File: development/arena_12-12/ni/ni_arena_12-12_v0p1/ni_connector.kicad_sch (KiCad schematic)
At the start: 1 part, among them J2 NI_TE_68pos

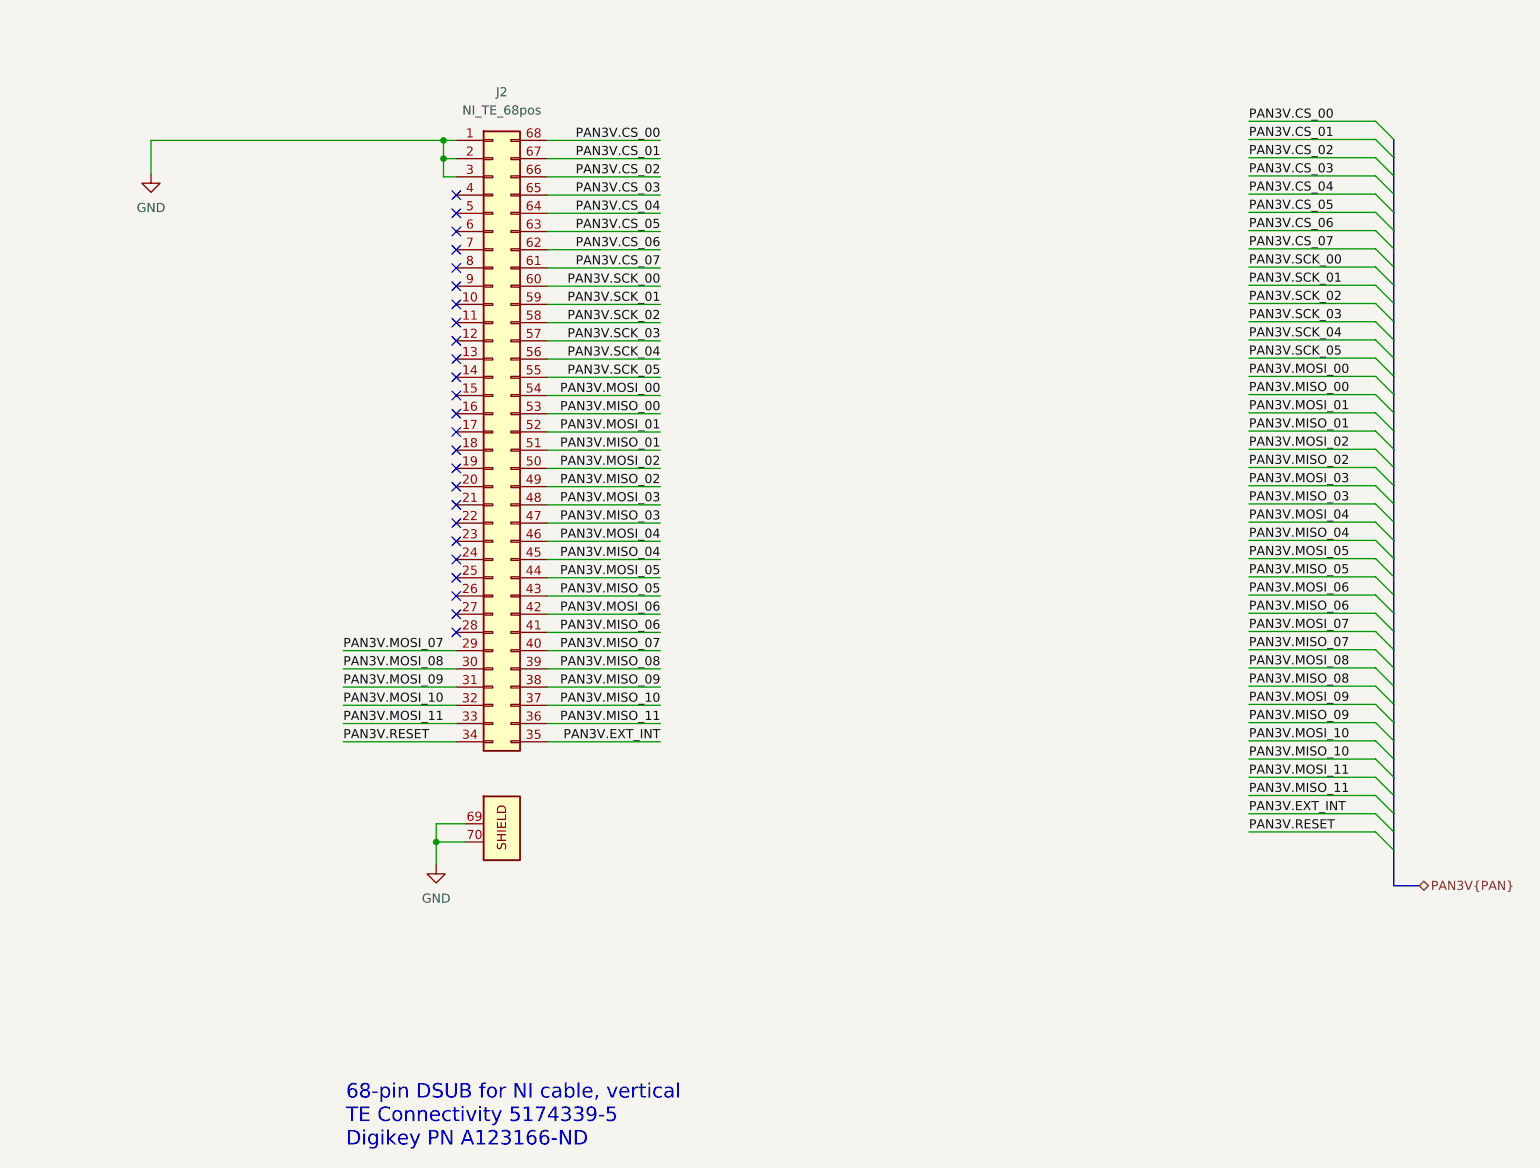
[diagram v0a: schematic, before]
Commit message: Worked on schematic adding series termination resistors and buffers.
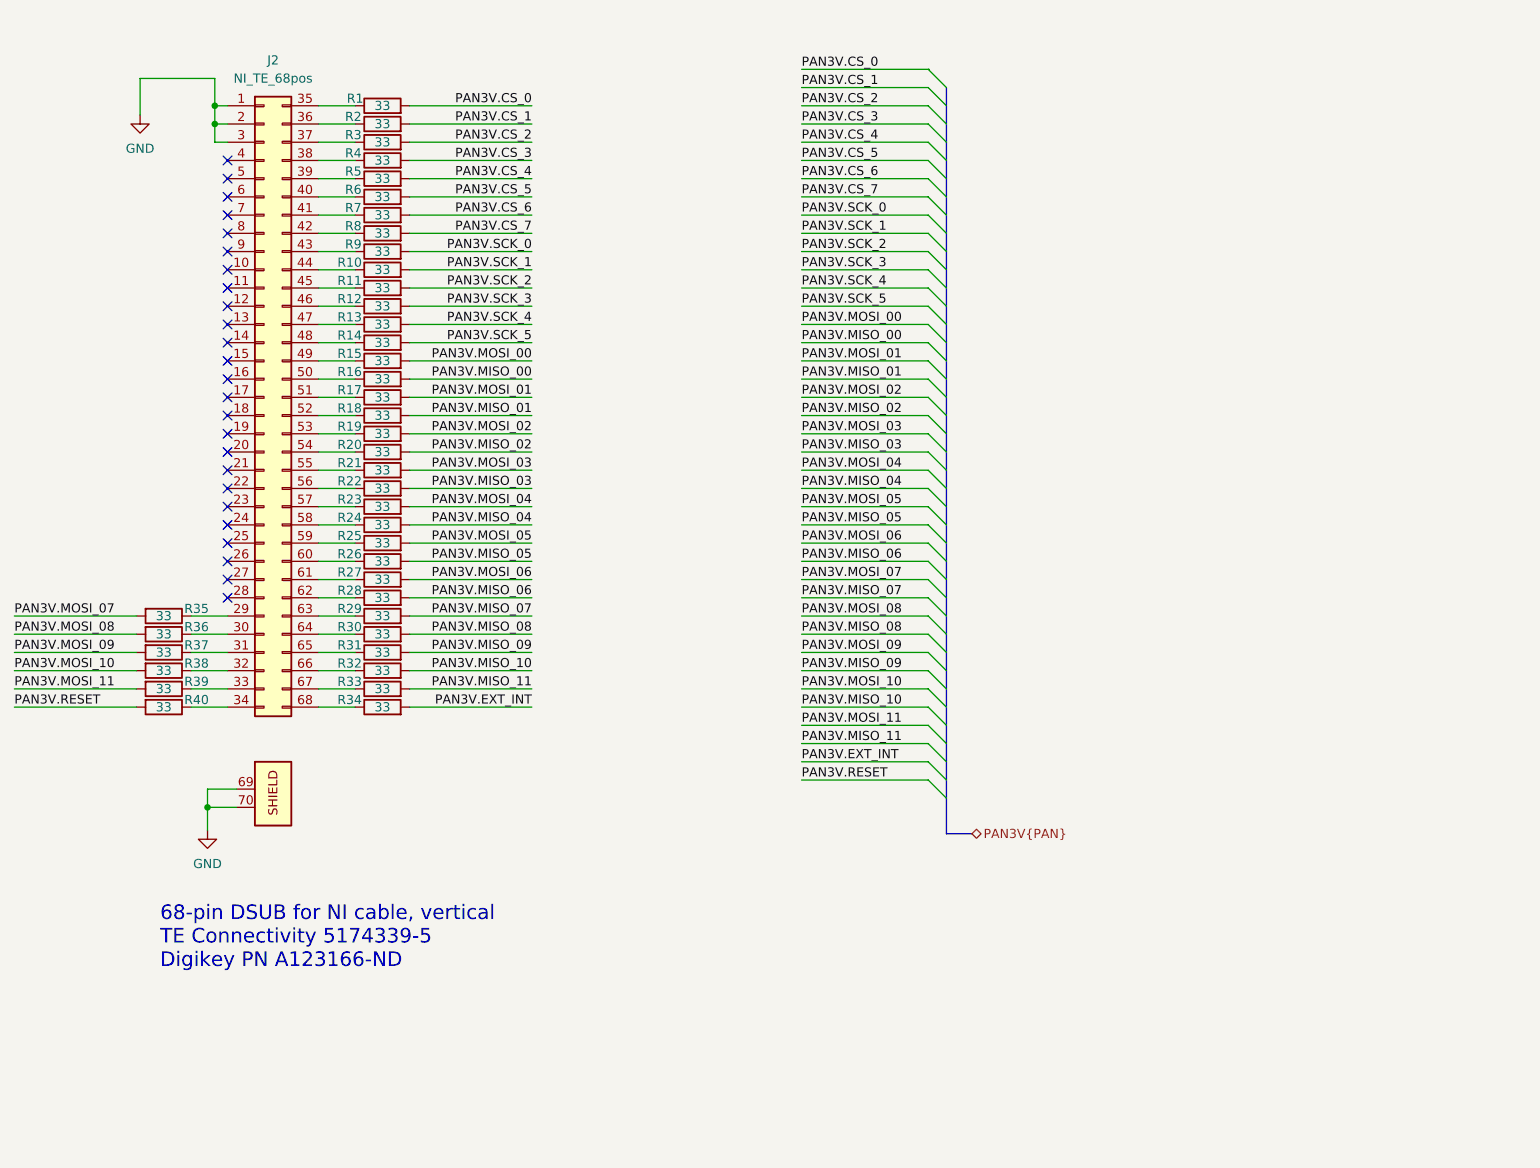
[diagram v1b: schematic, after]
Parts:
- added R1, R10, R11, R12, R13, R14, R15, R16, R17, R18, R19, R2, R20, R21, R22, R23, R24, R25, R26, R27, R28, R29, R3, R30, R31, R32, R33, R34, R35, R36, R37, R38, R39, R4, R40, R5, R6, R7, R8, R9: 33, symbol Device:R
- J2: footprint arena_custom:TE_CONN_DSUB_VERT_68 -> (none)
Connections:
- net PAN3V.EXT_INT: now also R34.2; no longer J2.35 (Pin_35)
- net PAN3V.MISO_00: now also R16.2; no longer J2.53 (Pin_53)
- net PAN3V.MISO_01: now also R18.2; no longer J2.51 (Pin_51)
- net PAN3V.MISO_02: now also R20.2; no longer J2.49 (Pin_49)
- net PAN3V.MISO_03: now also R22.2; no longer J2.47 (Pin_47)
- net PAN3V.MISO_04: now also R24.2; no longer J2.45 (Pin_45)
- net PAN3V.MISO_05: now also R26.2; no longer J2.43 (Pin_43)
- net PAN3V.MISO_06: now also R28.2; no longer J2.41 (Pin_41)
- net PAN3V.MISO_07: now also R29.2; no longer J2.40 (Pin_40)
- net PAN3V.MISO_08: now also R30.2; no longer J2.39 (Pin_39)
- net PAN3V.MISO_09: now also R31.2; no longer J2.38 (Pin_38)
- net PAN3V.MISO_10: now also R32.2; no longer J2.37 (Pin_37)
- net PAN3V.MISO_11: now also R33.2; no longer J2.36 (Pin_36)
- net PAN3V.MOSI_00: now also R15.2; no longer J2.54 (Pin_54)
- net PAN3V.MOSI_01: now also R17.2; no longer J2.52 (Pin_52)
- net PAN3V.MOSI_02: now also R19.2; no longer J2.50 (Pin_50)
- net PAN3V.MOSI_03: now also R21.2; no longer J2.48 (Pin_48)
- net PAN3V.MOSI_04: now also R23.2; no longer J2.46 (Pin_46)
- net PAN3V.MOSI_05: now also R25.2; no longer J2.44 (Pin_44)
- net PAN3V.MOSI_06: now also R27.2; no longer J2.42 (Pin_42)
- net PAN3V.MOSI_07: now also R35.2; no longer J2.29 (Pin_29)
- net PAN3V.MOSI_08: now also R36.2; no longer J2.30 (Pin_30)
- net PAN3V.MOSI_09: now also R37.2; no longer J2.31 (Pin_31)
- net PAN3V.MOSI_10: now also R38.2; no longer J2.32 (Pin_32)
- net PAN3V.MOSI_11: now also R39.2; no longer J2.33 (Pin_33)
- net PAN3V.RESET: now also R40.2; no longer J2.34 (Pin_34)
- net PAN3V.CS_00: no longer names the net of J2.68 (Pin_68)
- net PAN3V.CS_00: now also R34.1
- net PAN3V.CS_01: no longer names the net of J2.67 (Pin_67)
- net PAN3V.CS_01: now also R33.1
- net PAN3V.CS_02: no longer names the net of J2.66 (Pin_66)
- net PAN3V.CS_02: now also R32.1
- net PAN3V.CS_03: no longer names the net of J2.65 (Pin_65)
- net PAN3V.CS_03: now also R31.1
- net PAN3V.CS_04: no longer names the net of J2.64 (Pin_64)
- net PAN3V.CS_04: now also R30.1
- net PAN3V.CS_05: no longer names the net of J2.63 (Pin_63)
- net PAN3V.CS_05: now also R29.1
- net PAN3V.CS_06: no longer names the net of J2.62 (Pin_62)
- net PAN3V.CS_06: now also R28.1
- net PAN3V.CS_07: no longer names the net of J2.61 (Pin_61)
- net PAN3V.CS_07: now also R27.1
- net PAN3V.SCK_00: no longer names the net of J2.60 (Pin_60)
- net PAN3V.SCK_00: now also R26.1
- net PAN3V.SCK_01: no longer names the net of J2.59 (Pin_59)
- net PAN3V.SCK_01: now also R25.1
- net PAN3V.SCK_02: no longer names the net of J2.58 (Pin_58)
- net PAN3V.SCK_02: now also R24.1
- net PAN3V.SCK_03: no longer names the net of J2.57 (Pin_57)
- net PAN3V.SCK_03: now also R23.1
- net PAN3V.SCK_04: no longer names the net of J2.56 (Pin_56)
- net PAN3V.SCK_04: now also R22.1
- net PAN3V.SCK_05: no longer names the net of J2.55 (Pin_55)
- net PAN3V.SCK_05: now also R21.1
- new net: J2.37 (Pin_37), R3.1
- new net: J2.35 (Pin_35), R1.1
- new net: J2.41 (Pin_41), R7.1
- new net: J2.52 (Pin_52), R18.1
- new net: J2.48 (Pin_48), R14.1
- new net: J2.33 (Pin_33), R39.1
- new net: J2.50 (Pin_50), R16.1
- new net: J2.29 (Pin_29), R35.1
- new net: J2.30 (Pin_30), R36.1
- new net: J2.31 (Pin_31), R37.1
- new net: J2.32 (Pin_32), R38.1
- new net: J2.34 (Pin_34), R40.1
- new net: J2.36 (Pin_36), R2.1
- new net: J2.38 (Pin_38), R4.1
- new net: J2.39 (Pin_39), R5.1
- new net: J2.40 (Pin_40), R6.1
- new net: J2.42 (Pin_42), R8.1
- new net: J2.43 (Pin_43), R9.1
- new net: J2.44 (Pin_44), R10.1
- new net: J2.45 (Pin_45), R11.1
- new net: J2.46 (Pin_46), R12.1
- new net: J2.47 (Pin_47), R13.1
- new net: J2.49 (Pin_49), R15.1
- new net: J2.51 (Pin_51), R17.1
- new net: J2.53 (Pin_53), R19.1
- new net: J2.54 (Pin_54), R20.1
- new net PAN3V.CS_0: R1.2
- new net PAN3V.CS_1: R2.2
- new net PAN3V.CS_2: R3.2
- new net PAN3V.CS_3: R4.2
- new net PAN3V.CS_4: R5.2
- new net PAN3V.CS_5: R6.2
- new net PAN3V.CS_6: R7.2
- new net PAN3V.CS_7: R8.2
- new net PAN3V.SCK_0: R9.2
- new net PAN3V.SCK_1: R10.2
- new net PAN3V.SCK_2: R11.2
- new net PAN3V.SCK_3: R12.2
- new net PAN3V.SCK_4: R13.2
- new net PAN3V.SCK_5: R14.2

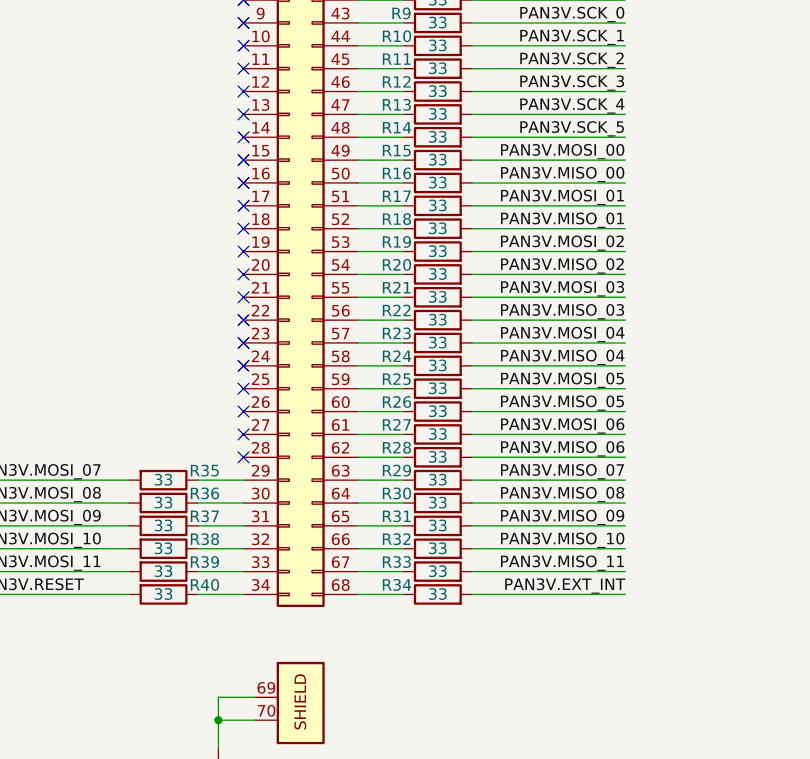
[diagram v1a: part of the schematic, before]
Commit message: Worked on 12-12 NI arena schematic.
Added schmitt trigger buffers and series termination resistors to
panels headers (not done).
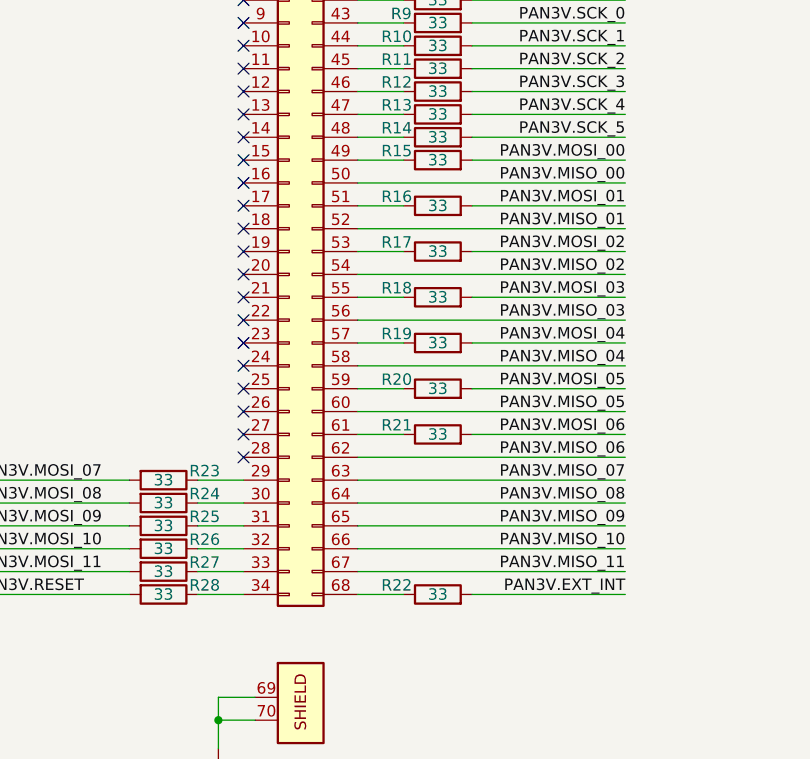
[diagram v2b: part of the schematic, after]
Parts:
- removed R16, R18, R20, R22, R24, R26, R28, R29, R30, R31, R32, R33: 33, symbol Device:R
- renumbered R17 to R16, R19 to R17, R21 to R18, R23 to R19, R25 to R20, R27 to R21, R34 to R22, R35 to R23, R36 to R24, R37 to R25, R38 to R26, R39 to R27, R40 to R28
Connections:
- net PAN3V.MISO_00: now also J2.50 (Pin_50)
- net PAN3V.MISO_01: now also J2.52 (Pin_52)
- net PAN3V.MISO_02: now also J2.54 (Pin_54)
- net PAN3V.MISO_03: now also J2.56 (Pin_56)
- net PAN3V.MISO_04: now also J2.58 (Pin_58)
- net PAN3V.MISO_05: now also J2.60 (Pin_60)
- net PAN3V.MISO_06: now also J2.62 (Pin_62)
- net PAN3V.MISO_07: now also J2.63 (Pin_63)
- net PAN3V.MISO_08: now also J2.64 (Pin_64)
- net PAN3V.MISO_09: now also J2.65 (Pin_65)
- net PAN3V.MISO_10: now also J2.66 (Pin_66)
- net PAN3V.MISO_11: now also J2.67 (Pin_67)

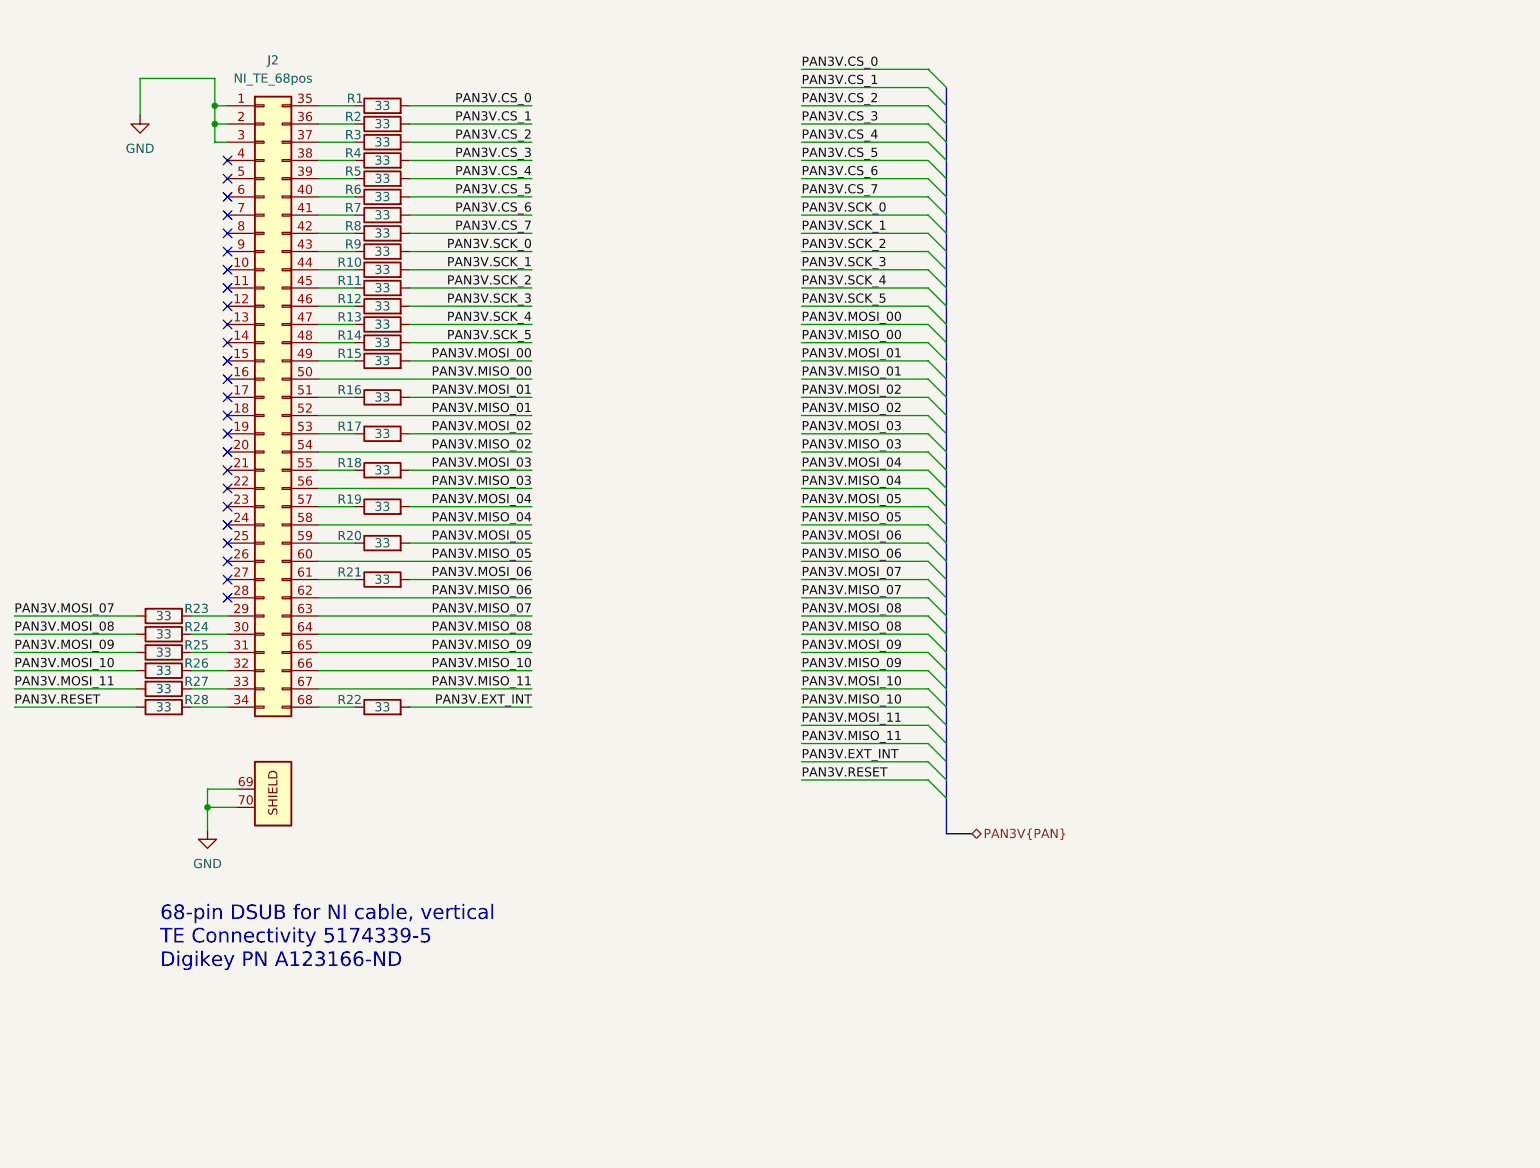
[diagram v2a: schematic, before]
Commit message: Finished initial schematic for 12-12 NI with schmitt buffers.
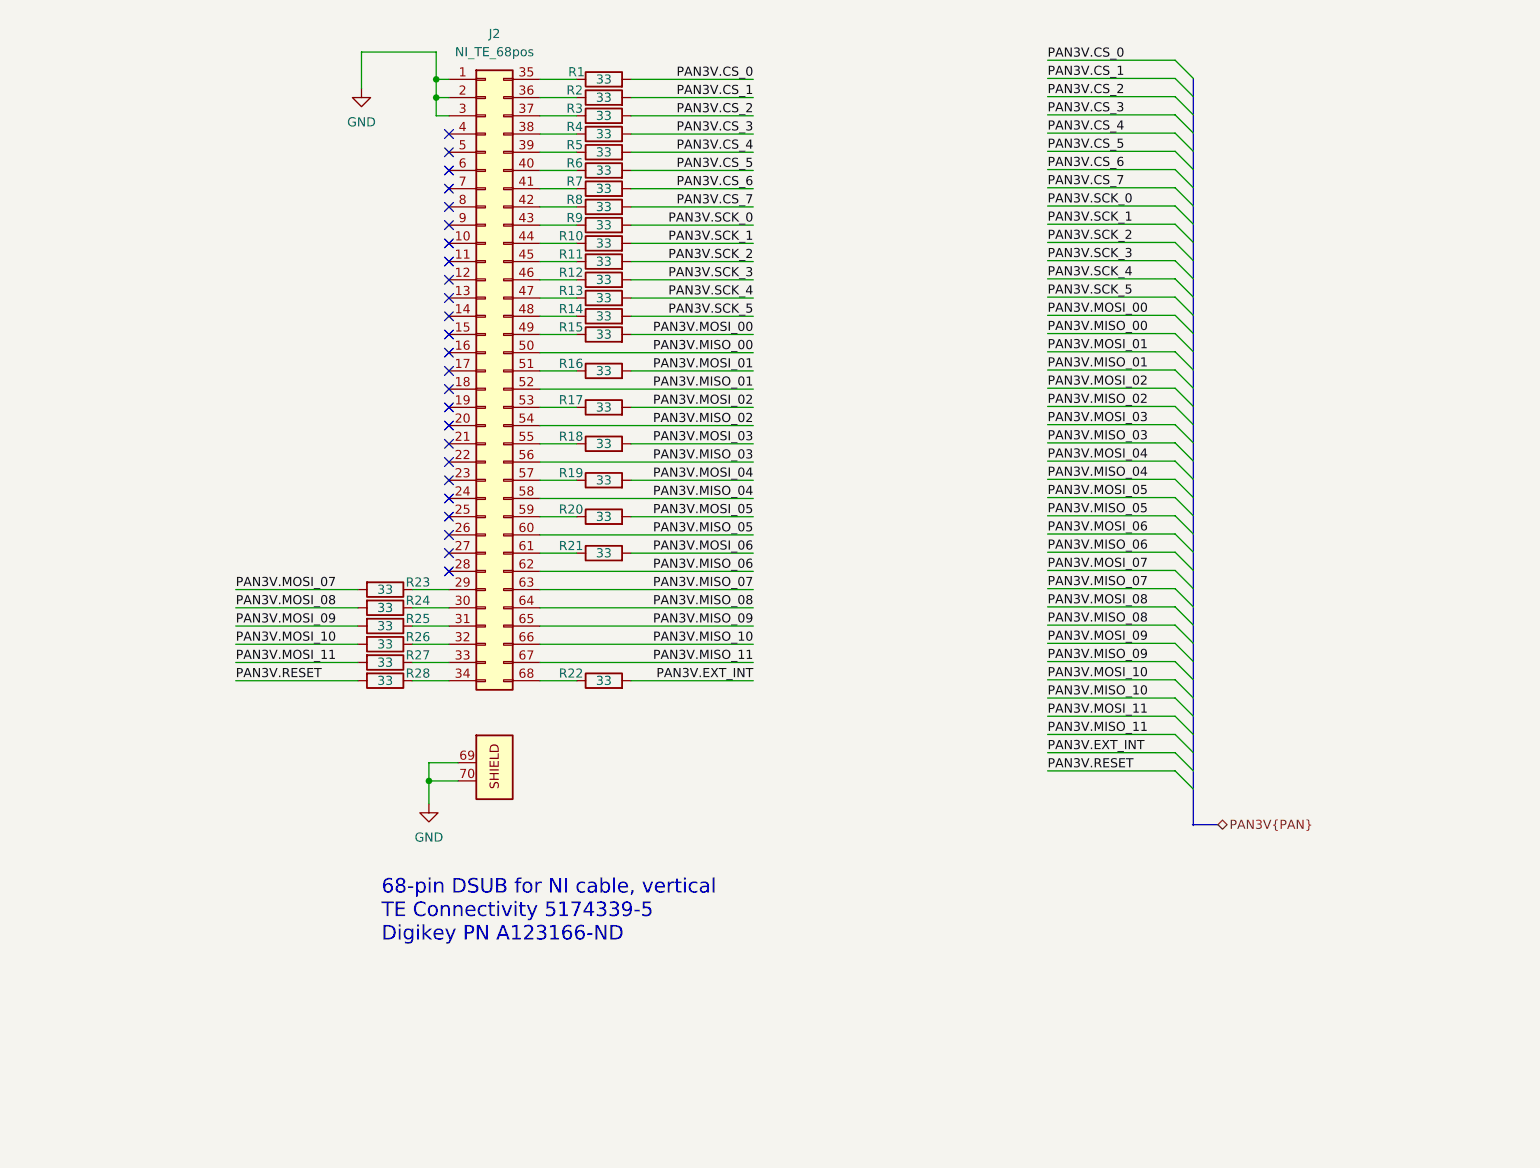
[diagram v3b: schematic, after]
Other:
- moved on the sheet: J2, R1, R10, R11, R12, R13, R14, R15, R16, R17, R18, R19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
